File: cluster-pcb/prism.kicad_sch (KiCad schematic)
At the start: 5 parts, among them J501 Conn_01x04_P3.5mm_TBH_Horizon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, U501 MAX13431E

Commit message: Update schematic
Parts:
- removed U501: MAX13431E, Janelia:21-0137I_T1033-1_MXM, symbol Janelia:MAX13431E
- added R502: 4.7k, Janelia:R_0402_1005Metric, symbol Janelia:R_4.7k_0402
- added U501: RS485, Janelia:DW0016B, symbol Janelia:Interface_RS485_ISO1410
- added U502: TPS1H200AQDGNRQ1, Janelia:SOP65P490X110-9N, symbol Janelia:TPS1H200AQDGNRQ1
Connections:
- net +3.3V: now also U501.1 (VCC1)
- net +5V: now also U501.16 (VCC2)
- net RX: now also U501.3 (RO)
- net SWN: now also U501.13 (B)
- net SWP: now also U501.12 (A)
- net TX: now also U501.6 (DI)
- net VAA: now also U502.8 (VS); no longer J501.4 (Pin_4)
- net GND renamed GND1
- net GND1: now also U501.10 (NC), U501.11 (NC), U501.14 (NC), U501.15 (GND2), U501.2 (GND1), U501.7 (NC), U501.8 (GND1), U501.9 (GND2), U502.2 (DIAG_EN), U502.4 (CL), U502.5 (DELAY), U502.6 (GND), U502.9 (EP)
- new net: R502.2, U502.1 (IN)
- new net ENABLE_POWER: R502.1
- new net ENABLE_TXRX: U501.4 (~{RE}), U501.5 (DE)
- new net VBB: J501.4 (Pin_4), U502.7 (OUT)
- no-connect marks 0 -> 1
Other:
- moved on the sheet: C501, C502, J501, R501

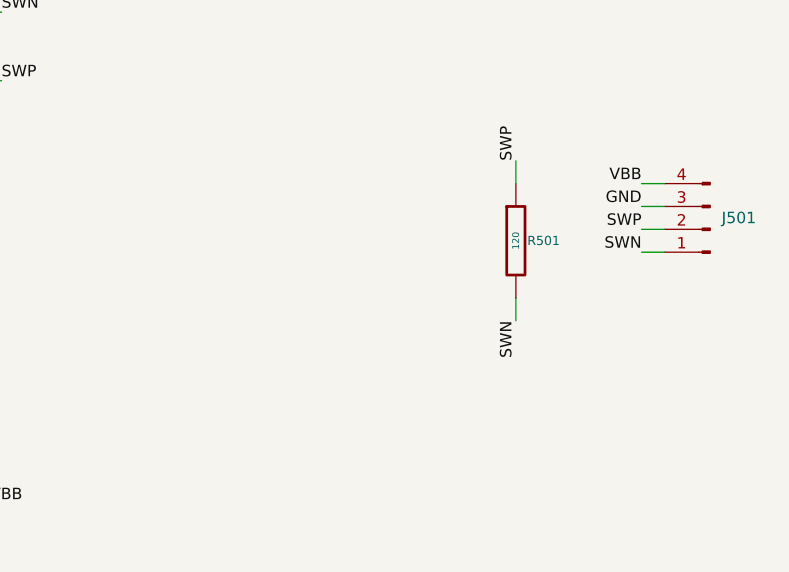
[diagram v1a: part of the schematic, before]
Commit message: Fix ERC issues
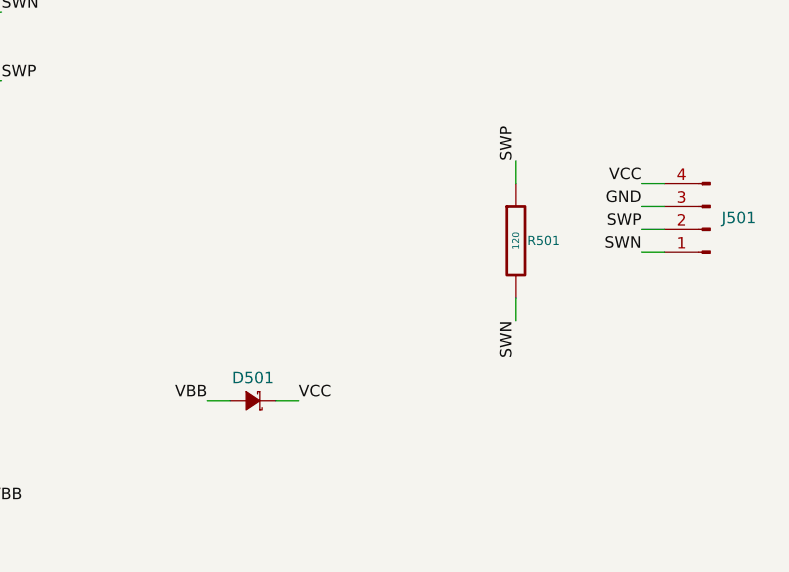
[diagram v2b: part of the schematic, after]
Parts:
- added D501: D_SCHOTTKY_20V_1A, Janelia:SOD-123FL, symbol Janelia:D_SCHOTTKY_60V_3A
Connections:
- net VBB: now also D501.2 (A); no longer J501.4 (Pin_4)
- net GND1 renamed GND
- new net VCC: D501.1 (K), J501.4 (Pin_4)
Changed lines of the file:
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@@
   (title_block
     (title "cluster-pcb")
-    (date "2024-09-12")
+    (date "2024-09-13")
     (rev "1.2")
     (company "Howard Hughes Medical Institute")
@@
     (stroke (width 0) (type default))
   )
+  (wire (pts (xy 175.26 118.11) (xy 172.72 118.11))
+    (stroke (width 0) (type default))
+  )
   (wire (pts (xy 119.38 77.47) (xy 121.92 77.47))
     (stroke (width 0) (type default))
   )
+  (wire (pts (xy 180.34 118.11) (xy 182.88 118.11))
+    (stroke (width 0) (type default))
+  )
   (wire (pts (xy 207.01 93.98) (xy 207.01 91.44))
     (stroke (width 0) (type default))
@@
     (effects (font (size 1.27 1.27)) (justify left bottom))
   )
-  (label "VBB" (at 220.98 93.98 180) (fields_autoplaced)
-    (effects (font (size 1.27 1.27)) (justify right bottom))
+  (label "VCC" (at 220.98 93.98 180) (fields_autoplaced)
+    (effects (font (size 1.27 1.27)) (justify right bottom))
+  )
+  (label "VCC" (at 182.88 118.11 0) (fields_autoplaced)
+    (effects (font (size 1.27 1.27)) (justify left bottom))
   )
   (label "SWN" (at 207.01 109.22 270) (fields_autoplaced)
@@
   )
   (label "SWN" (at 220.98 101.6 180) (fields_autoplaced)
+    (effects (font (size 1.27 1.27)) (justify right bottom))
+  )
+  (label "VBB" (at 172.72 118.11 180) (fields_autoplaced)
     (effects (font (size 1.27 1.27)) (justify right bottom))
   )
@@
         )
       )
+    )
+  )
+  (symbol (lib_id "Janelia:D_SCHOTTKY_60V_3A") (at 177.8 118.11 180) (unit 1)
+    (in_bom yes) (on_board yes) (dnp no)
+    (property "Reference" "D501" (at 177.8 115.57 0)
+      (effects (font (size 1.27 1.27)))
+    )
+    (property "Value" "D_SCHOTTKY_20V_1A" (at 184.912 116.078 0)
+      (effects (font (size 1.27 1.27)) (justify left) hide)
+    )
+    (property "Footprint" "Janelia:SOD-123FL" (at 181.61 117.602 0)
+      (effects (font (size 1.524 1.524)) hide)
+    )
+    (property "Datasheet" "" (at 179.07 120.142 0)
+      (effects (font (size 1.524 1.524)) hide)
+    )
+    (property "Vendor" "JLCPCB" (at 176.53 122.682 0)
+      (effects (font (size 1.524 1.524)) hide)
+    )
+    (property "Vendor Part Number" "C106913" (at 173.99 125.222 0)
+      (effects (font (size 1.524 1.524)) hide)
+    )
+    (property "Synopsis" "DIODE SCHOTTKY 60V 3A" (at 171.45 127.762 0)
+      (effects (font (size 1.524 1.524)) hide)
+    )
+    (property "Manufacturer" "MDD(Microdiode Semiconductor)" (at 177.8 118.11 0)
+      (effects (font (size 1.27 1.27)) hide)
+    )
+    (property "Manufacturer Part Number" "DSK36" (at 177.8 118.11 0)
+      (effects (font (size 1.27 1.27)) hide)
+    )
+    (property "Package" "SOD-123FL" (at 177.8 118.11 0)
+      (effects (font (size 1.27 1.27)) hide)
+    )
+    (property "Sim.Enable" "0" (at 177.8 118.11 0)
+      (effects (font (size 1.27 1.27)) hide)
+    )
+    (property "LCSC" "C106913" (at 177.8 118.11 0)
+      (effects (font (size 1.27 1.27)) hide)
+    )
+    (pin "1")
+    (pin "2")
+    (instances
+      (project "cluster-pcb"
+        (path "/df2b2e89-e055-4140-95de-f1df723db034/622b6afe-64ba-4b4f-894e-aa16e3fefe2c"
+          (reference "D501") (unit 1)
+        )
+        (path "/df2b2e89-e055-4140-95de-f1df723db034/a71d32da-f9cb-43f1-ab25-5fee9e3817d5"
+          (reference "D601") (unit 1)
+        )
+        (path "/df2b2e89-e055-4140-95de-f1df723db034/9d4d3b5f-be88-4261-b203-2246a336433c"
+          (reference "D701") (unit 1)
+        )
+        (path "/df2b2e89-e055-4140-95de-f1df723db034/db5894f8-55af-48c2-a941-3e31d7793716"
+          (reference "D801") (unit 1)
+        )
+        (path "/df2b2e89-e055-4140-95de-f1df723db034/6d3bcc59-228e-43b3-9299-2dd708dcaa45"
+          (reference "D901") (unit 1)
+        )
+        (path "/df2b2e89-e055-4140-95de-f1df723db034/bfbaa572-51ae-4b71-8c7f-4f186195adbc"
+          (reference "D1001") (unit 1)
+        )
+        (path "/df2b2e89-e055-4140-95de-f1df723db034/78ebced8-6951-4549-97f4-07e6588cf891"
+          (reference "D1101") (unit 1)
+        )
+      )

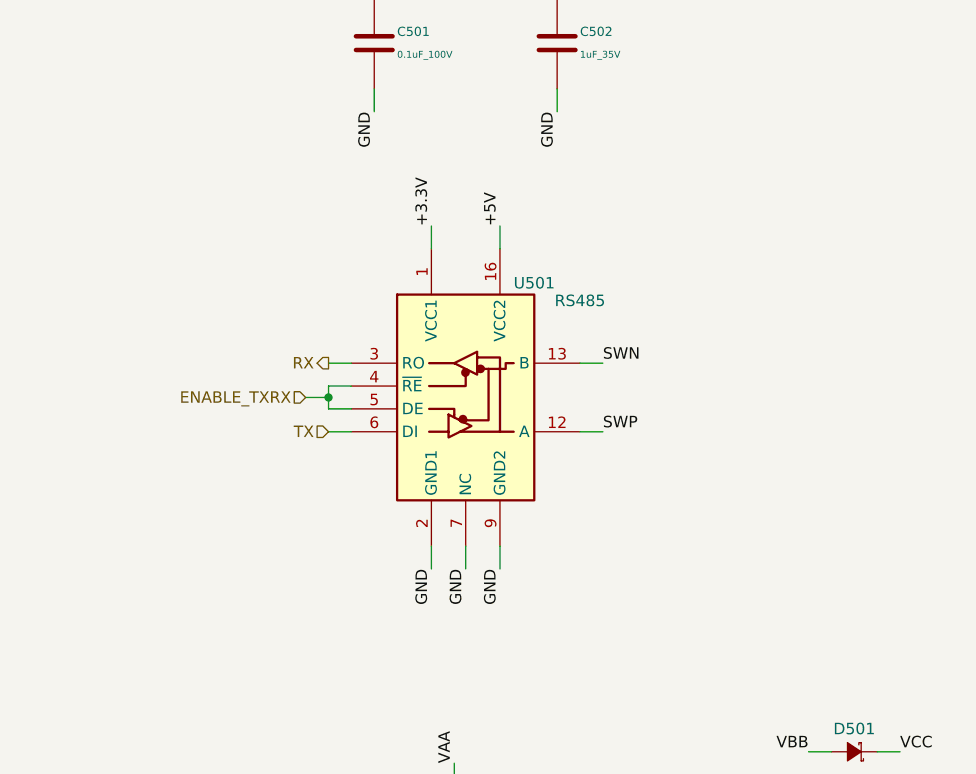
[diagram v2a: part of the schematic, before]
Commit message: Rearrange footprints
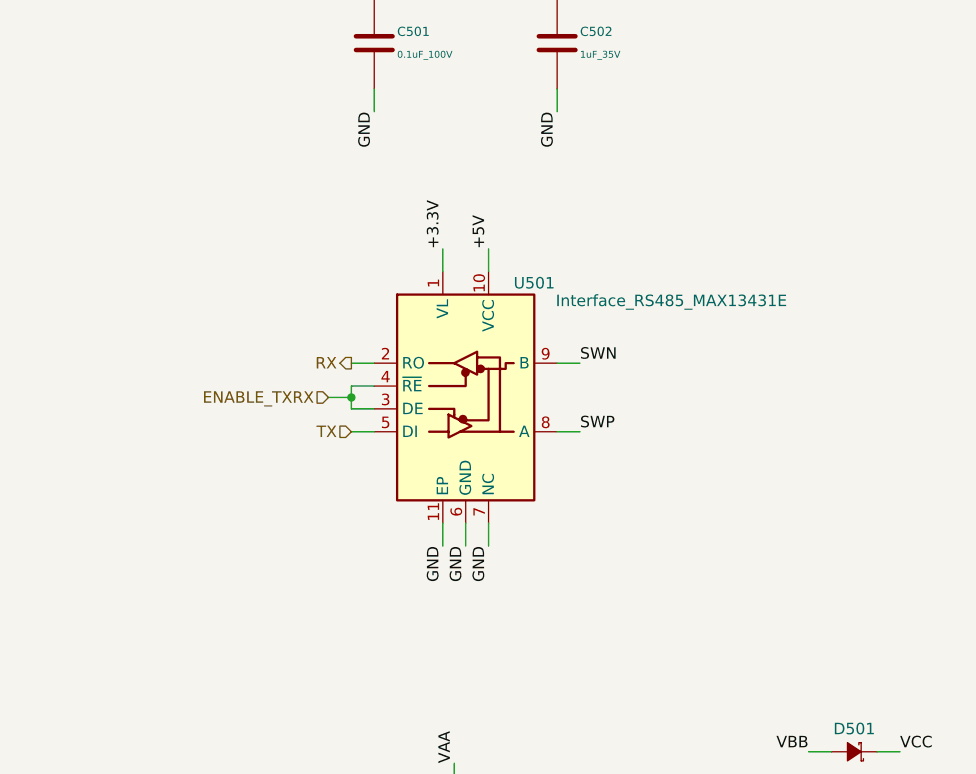
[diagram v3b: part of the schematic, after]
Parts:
- removed U501: RS485, Janelia:DW0016B, symbol Janelia:Interface_RS485_ISO1410
- added U501: Interface_RS485_MAX13431E, Janelia:21-0137I_T1033-1_MXM, symbol Janelia:Interface_RS485_MAX13431E
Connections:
- net +3.3V: now also U501.1 (VL)
- net +5V: now also U501.10 (VCC)
- net ENABLE_TXRX: now also U501.3 (DE), U501.4 (~{RE})
- net GND: now also U501.11 (EP), U501.6 (GND), U501.7 (NC)
- net RX: now also U501.2 (RO)
- net SWN: now also U501.9 (B)
- net SWP: now also U501.8 (A)
- net TX: now also U501.5 (DI)

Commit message: Finish routing
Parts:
- removed J501: Conn_01x04_P3.5mm_TBH_Horizontal_Screw, Janelia:PhoenixContact_MC_1,5_4-G-3.5_1x04_P3.50mm_Horizontal_Screw, symbol Janelia:Conn_01x04_P3.5mm_TBH_Horizontal_Screw
- removed R501: 120, Janelia:R_0402_1005Metric, symbol Janelia:R_120_0402
- added J501: Connector_USB_C_Receptacle_USB2.0_16P_GT-USB-7047C, Janelia:USB_C_Receptacle_GT-USB-7047C_16P_TopMnt_Horizontal, symbol Janelia:Connector_USB_C_Receptacle_USB2.0_16P_GT-USB-7047C
- added R501: 100, Janelia:R_0402_1005Metric, symbol Janelia:R_100_0402
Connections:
- net GND: now also J501.A1 (GND), J501.A12 (GND), J501.B1 (GND), J501.B12 (GND), J501.S1 (SHIELD)
- net SWN: now also J501.A7 (D-), J501.B7 (D-), R501.2
- net SWP: now also J501.A6 (D+), J501.B6 (D+), R501.1
- net VCC: now also J501.A4 (VBUS), J501.A9 (VBUS), J501.B4 (VBUS), J501.B9 (VBUS)
- no-connect marks 1 -> 5
